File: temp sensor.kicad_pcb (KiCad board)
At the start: 2 copper layers, 48.2 x 24.9 mm, 36 parts, among them IC1 ESP32-C3-MINI-1, J2 Conn_01x04_Male, J3 Conn_01x05_Male, J4 USB_B_Micro, U1 SHTC3, U2 TLV62569DBV, U3 BME280, U4 Si7020-A20, U5 SN65220

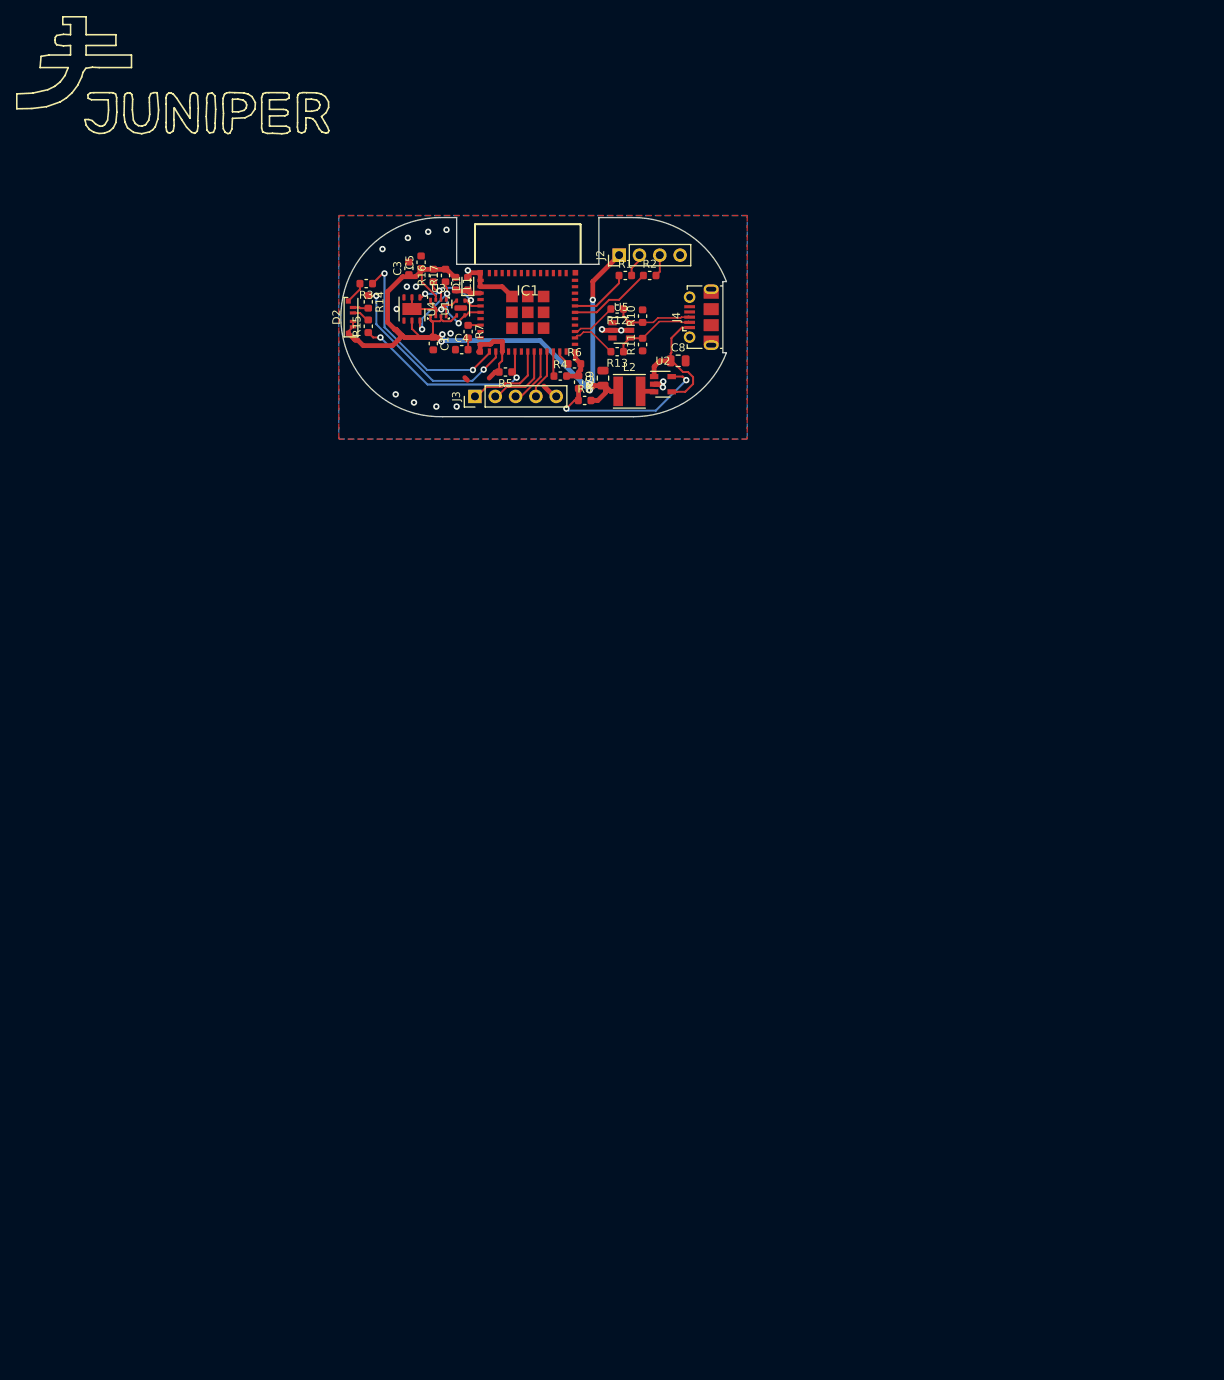
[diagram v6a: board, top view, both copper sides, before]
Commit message: lots of layout changes, optimized RF pathway, adjusted pinout, still working on ESP32 pinout
Signed-off-by: lokimetasmith <lokimail@gmail.com>
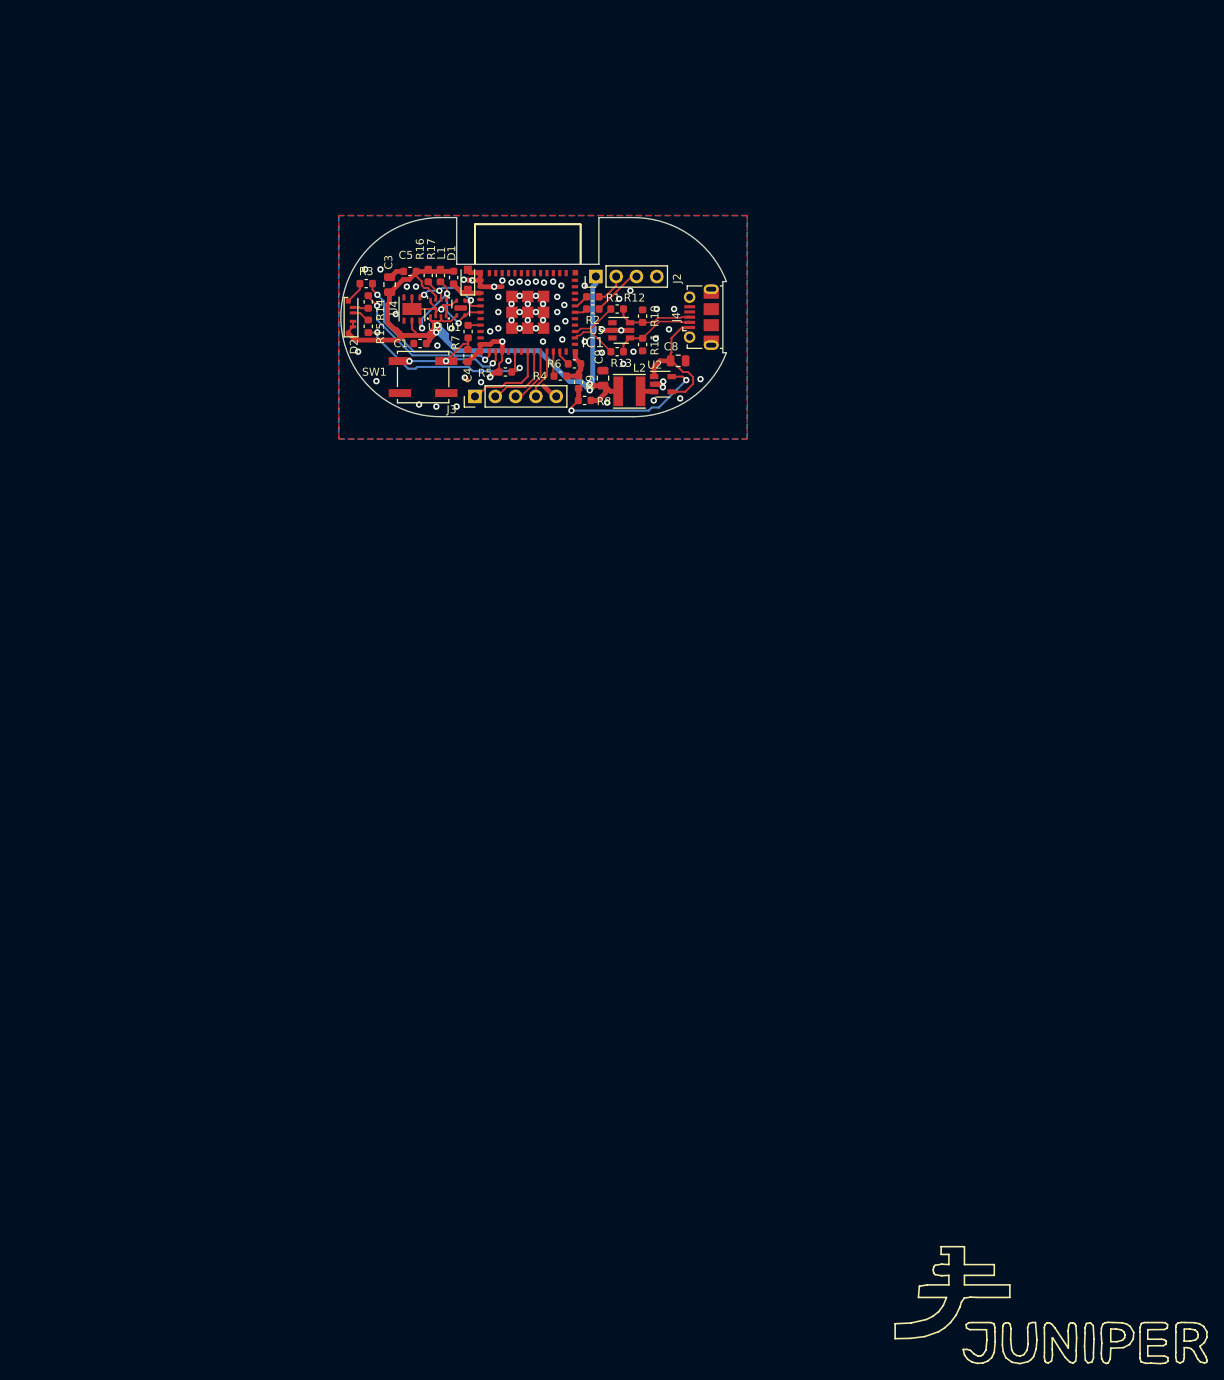
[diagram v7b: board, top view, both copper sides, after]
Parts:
- added SW1: SW_Push, Button_Switch_SMD:SW_Push_1P1T_NO_CK_KSC6xxJ, F.Cu at (63.6, 58.3)
- C3: footprint Capacitor_SMD:C_0603_1608Metric -> Capacitor_SMD:C_0805_2012Metric
- D1: footprint Diode_SMD:D_0603_1608Metric -> Diode_SMD:D_SOD-323_HandSoldering
- moved R2 8.25 mm to (84.8, 49.8)
- moved R1 4.86 mm to (84.8, 48.3)
- moved J2 3.95 mm to (85.2, 45.7)
- moved C3 3.15 mm to (59.4, 46.7)
- moved C5 1.81 mm to (62.0, 45.1), turned to 180 degrees
- moved C1 1.65 mm to (63.2, 54.1), turned to 180 degrees
- moved C4 1.08 mm to (69.2, 55.6), turned to 90 degrees
- moved L1 0.80 mm to (67.4, 45.8)
- moved R16 0.64 mm to (64.3, 45.6)
- moved R17 0.64 mm to (65.8, 45.6)
- moved D1 0.49 mm to (69.2, 46.1)
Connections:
- IC1 pad 10: Net-(IC1-Pad10) -> (no net)
- IC1 pad 15: Net-(IC1-Pad15) -> (no net)
- IC1 pad 17: Net-(IC1-Pad17) -> (no net)
- IC1 pad 24: Net-(IC1-Pad24) -> (no net)
- IC1 pad 25: Net-(IC1-Pad25) -> (no net)
- IC1 pad 28: Net-(IC1-Pad28) -> (no net)
- IC1 pad 29: Net-(IC1-Pad29) -> (no net)
- IC1 pad 32: Net-(IC1-Pad32) -> (no net)
- IC1 pad 33: Net-(IC1-Pad33) -> (no net)
- IC1 pad 34: Net-(IC1-Pad34) -> (no net)
- IC1 pad 35: Net-(IC1-Pad35) -> (no net)
- IC1 pad 4: Net-(IC1-Pad4) -> (no net)
- IC1 pad 7: Net-(IC1-Pad7) -> (no net)
- IC1 pad 9: Net-(IC1-Pad9) -> (no net)
- J4 pad 4: Net-(J4-Pad4) -> (no net)
- U1 pad 5: Net-(U1-Pad5) -> (no net)
- U4 pad 3: Net-(U4-Pad3) -> (no net)
- U4 pad 4: Net-(U4-Pad4) -> (no net)
- U5 pad 1: Net-(U5-Pad1) -> (no net)
- U5 pad 3: Net-(U5-Pad3) -> (no net)
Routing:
- net Net-(C4-Pad2): track 1.75 -> 11.7 mm, vias 0 -> 2
- net Net-(IC1-Pad30): track 10.5 -> 1.61 mm
- net Net-(IC1-Pad31): track 7.65 -> 1.82 mm
- net GND: track 44.8 -> 49.2 mm, vias 18 -> 71
- net /io0: track 25.2 -> 21.2 mm
- net +3V3: track 103.6 -> 99.9 mm, vias 5 -> 4
- net /RTX0: track 2.74 -> 6.36 mm
- net /io1: track 24.4 -> 22.2 mm
- net /3v3: track 3.23 -> 4.81 mm
- net Net-(R8-Pad1): track 22.1 -> 21.1 mm
- net /TDX0: track 2.95 -> 3.86 mm

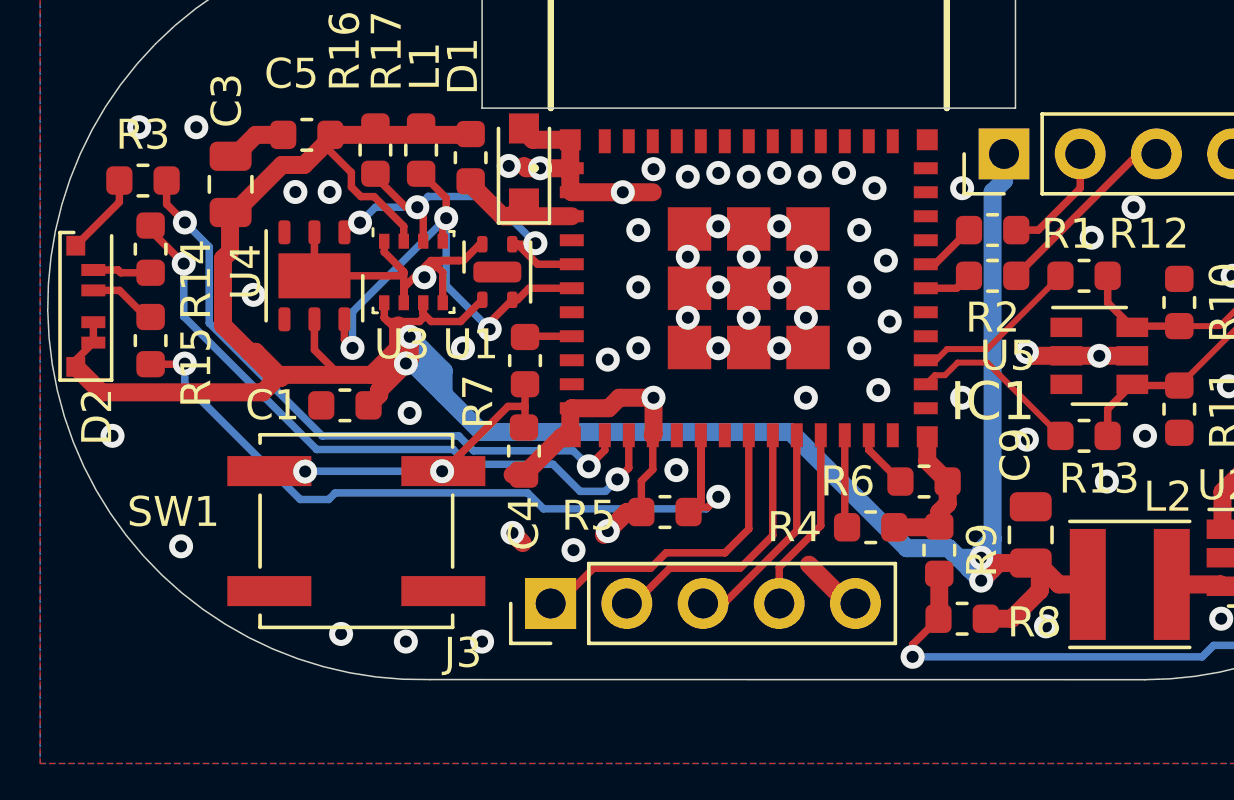
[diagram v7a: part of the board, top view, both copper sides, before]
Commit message: updated schematic for updated parts
Signed-off-by: lokimetasmith <lokimail@gmail.com>
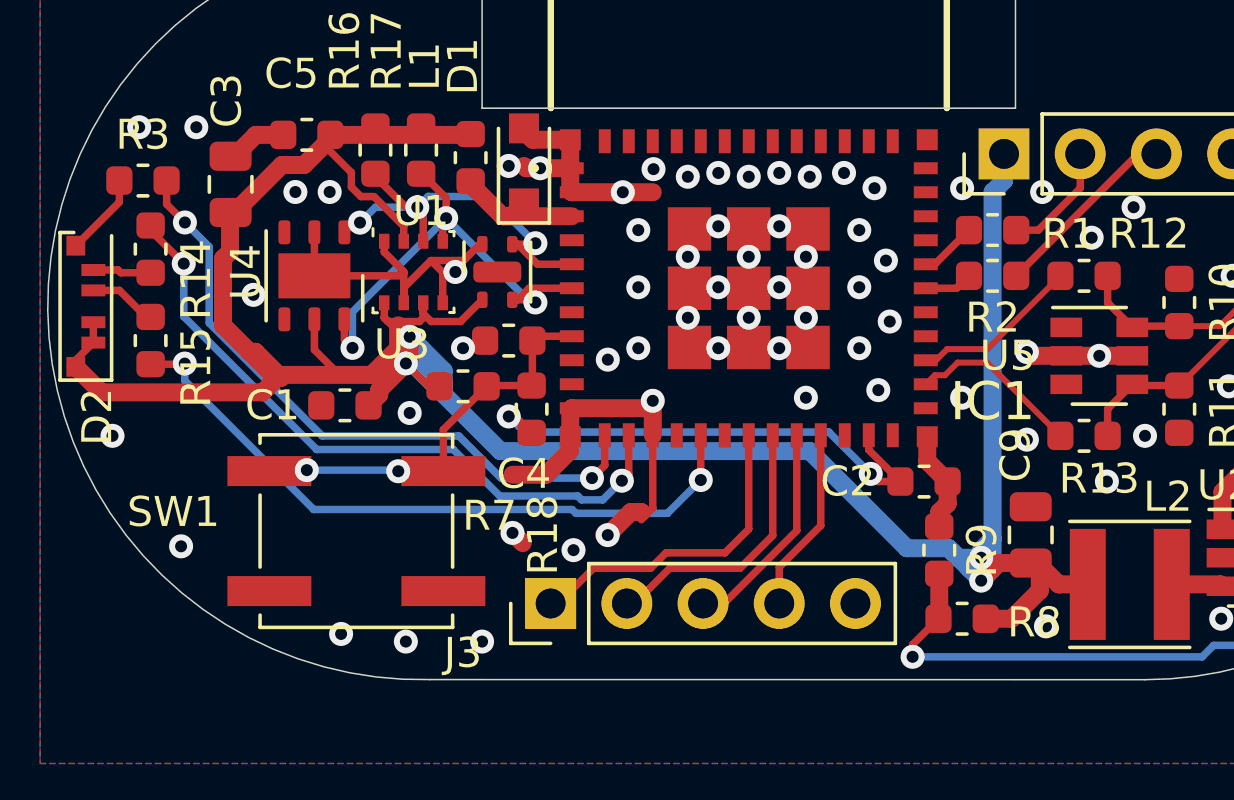
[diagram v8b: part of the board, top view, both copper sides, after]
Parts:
- removed R4, R5, R6: 10K, Resistor_SMD:R_0603_1608Metric
- added C2: 0.1u, Capacitor_SMD:C_0603_1608Metric, F.Cu at (82.5, 56.6)
- added R18: 2.2K, Resistor_SMD:R_0603_1608Metric, F.Cu at (69.5, 54.2)
- C4: value 1u -> 0.1u
- moved C4 3.72 mm to (68.7, 51.9), turned to 0 degrees
- moved R7 2.24 mm to (67.2, 53.5), turned to 180 degrees
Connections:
- C4 pad 2: Net-(C4-Pad2) -> /EN
- IC1 pad 22: Net-(IC1-Pad22) -> (no net)
- R7 pad 2: Net-(C4-Pad2) -> +3V3
- SW1 pad 2: Net-(C4-Pad2) -> /EN
- U1 pad 5: (no net) -> GND
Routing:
- net /Boot_Option: track 1.98 -> 16.9 mm, vias 0 -> 2
- net /EN: track 1.89 -> 14.2 mm, vias 0 -> 2
- net Net-(C4-Pad2): track 11.7 -> 0.00 mm, vias 2 -> 0
- net /io10: track 28.7 -> 22.7 mm
- net GND: track 49.2 -> 44.5 mm
- net Net-(IC1-Pad22): track 3.10 -> 0.00 mm
- net +3V3: track 99.9 -> 101.4 mm
- net /SCL: track 17.1 -> 16.4 mm
- net /io0: track 21.2 -> 21.8 mm
